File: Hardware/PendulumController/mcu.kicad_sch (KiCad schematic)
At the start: 21 parts, among them J201 ICSP, SW201 RESET, SW202 START_SW, SW203 STOP/MODE_SW, U201 ATmega328P, Y201 16mHz

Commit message: Fix DRC check
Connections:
- net SCL: no longer names the net of U201.28 (PC5)
- net SDA: no longer names the net of U201.27 (PC4)
- no-connect marks 7 -> 9
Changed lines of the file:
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@@
   (junction (at 59.69 86.995) (diameter 0) (color 0 0 0 0)
   )
+  (no_connect (at 57.785 81.915))
   (no_connect (at 27.305 56.515))
+  (no_connect (at 57.785 84.455))
   (no_connect (at 48.26 154.94))
   (no_connect (at 48.26 157.48))
@@
     (stroke (width 0) (type default) (color 0 0 0 0))
   )
-  (wire (pts (xy 66.675 84.455) (xy 57.785 84.455))
-    (stroke (width 0) (type default) (color 0 0 0 0))
-  )
   (wire (pts (xy 129.54 73.025) (xy 129.54 73.66))
     (stroke (width 0) (type default) (color 0 0 0 0))
@@
   )
   (polyline (pts (xy 13.335 173.355) (xy 64.77 173.355))
-    (stroke (width 0) (type default) (color 0 0 0 0))
-  )
-  (wire (pts (xy 66.675 81.915) (xy 57.785 81.915))
     (stroke (width 0) (type default) (color 0 0 0 0))
   )
@@
     (effects (font (size 1.27 1.27)) (justify right))
   )
-  (hierarchical_label "SCL" (shape output) (at 66.675 84.455 0)
-    (effects (font (size 1.27 1.27)) (justify left))
-  )
   (hierarchical_label "TFT_CS" (shape output) (at 81.28 104.775 0)
     (effects (font (size 1.27 1.27)) (justify left))
@@
     (effects (font (size 1.27 1.27)) (justify left))
   )
-  (hierarchical_label "SDA" (shape bidirectional) (at 66.675 81.915 0)
-    (effects (font (size 1.27 1.27)) (justify left))
-  )

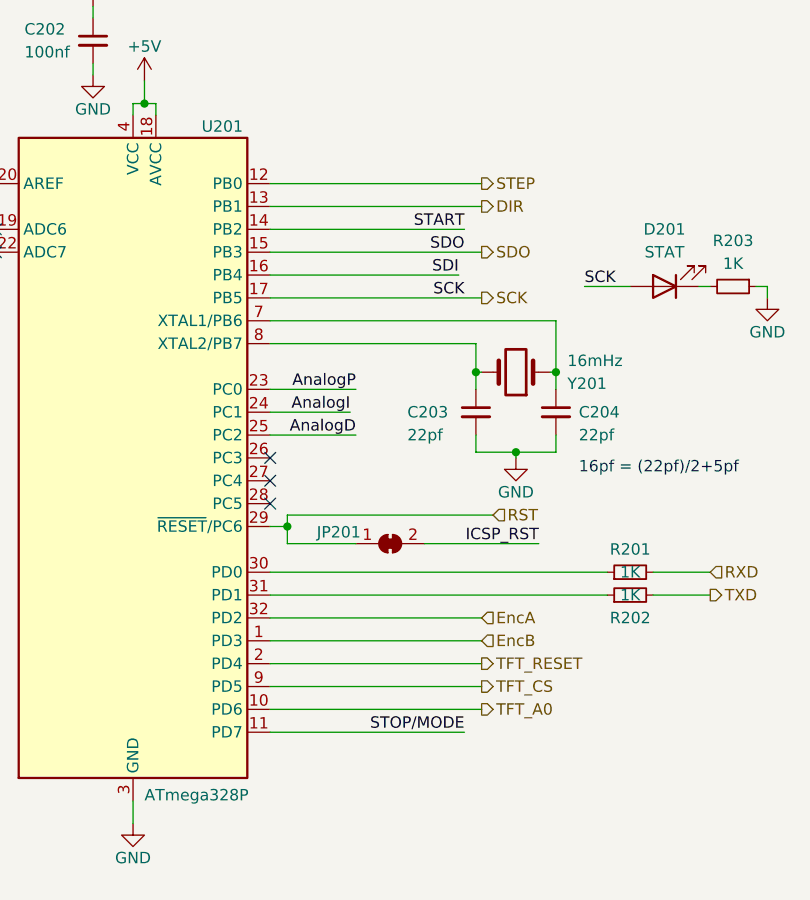
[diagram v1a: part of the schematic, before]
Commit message: Check backlight power circuit before printing
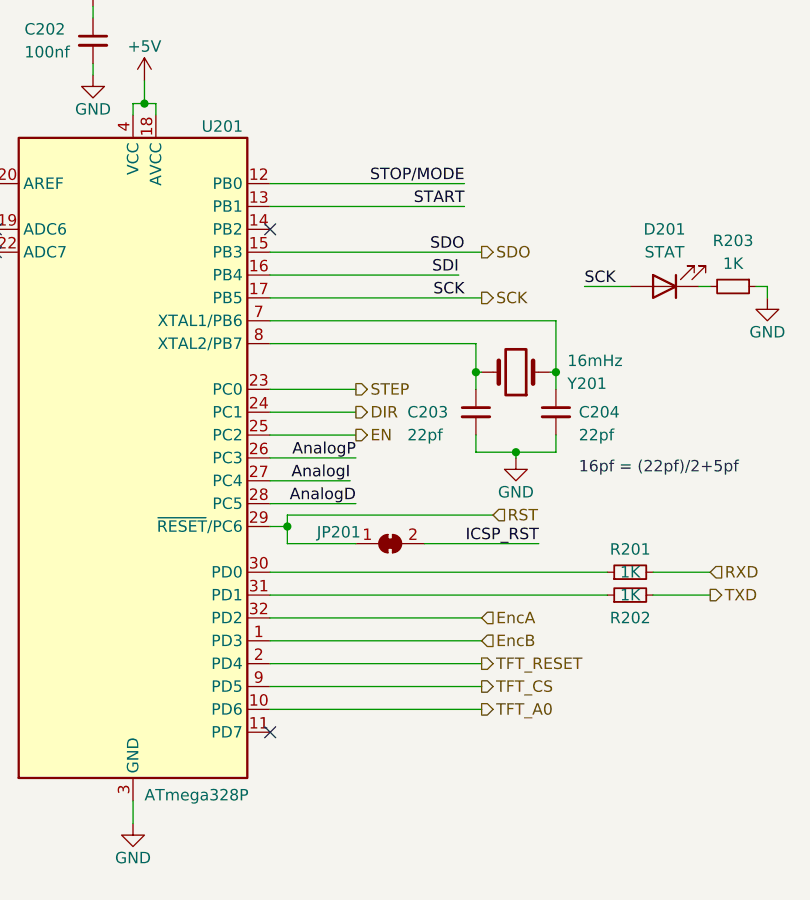
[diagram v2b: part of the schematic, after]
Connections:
- net AnalogD: now also U201.28 (PC5); no longer U201.25 (PC2)
- net AnalogI: now also U201.27 (PC4); no longer U201.24 (PC1)
- net AnalogP: now also U201.26 (PC3); no longer U201.23 (PC0)
- net DIR: now also U201.24 (PC1); no longer U201.13 (PB1)
- net START: now also U201.13 (PB1); no longer U201.14 (PB2)
- net STEP: now also U201.23 (PC0); no longer U201.12 (PB0)
- net STOP/MODE: now also U201.12 (PB0); no longer U201.11 (PD7)
- new net EN: U201.25 (PC2)
- no-connect marks 9 -> 8
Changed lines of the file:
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@@
   (junction (at 59.69 86.995) (diameter 0) (color 0 0 0 0)
   )
-  (no_connect (at 57.785 81.915))
   (no_connect (at 27.305 56.515))
-  (no_connect (at 57.785 84.455))
   (no_connect (at 48.26 154.94))
+  (no_connect (at 57.785 53.975))
+  (no_connect (at 57.785 109.855))
   (no_connect (at 48.26 157.48))
   (no_connect (at 48.26 152.4))
   (no_connect (at 35.56 152.4))
-  (no_connect (at 57.785 79.375))
   (no_connect (at 27.305 53.975))
-  (wire (pts (xy 57.785 48.895) (xy 81.28 48.895))
-    (stroke (width 0) (type default) (color 0 0 0 0))
-  )
   (wire (pts (xy 129.54 92.075) (xy 129.54 93.345))
     (stroke (width 0) (type default) (color 0 0 0 0))
@@
     (stroke (width 0) (type default) (color 0 0 0 0))
   )
-  (wire (pts (xy 57.785 71.755) (xy 67.31 71.755))
-    (stroke (width 0) (type default) (color 0 0 0 0))
-  )
   (wire (pts (xy 23.495 56.515) (xy 23.495 59.055))
     (stroke (width 0) (type default) (color 0 0 0 0))
   )
-  (wire (pts (xy 57.785 51.435) (xy 81.28 51.435))
-    (stroke (width 0) (type default) (color 0 0 0 0))
-  )
   (wire (pts (xy 45.085 40.005) (xy 43.815 40.005))
     (stroke (width 0) (type default) (color 0 0 0 0))
@@
     (stroke (width 0) (type default) (color 0 0 0 0))
   )
+  (wire (pts (xy 57.785 51.435) (xy 79.375 51.435))
+    (stroke (width 0) (type default) (color 0 0 0 0))
+  )
   (wire (pts (xy 80.645 69.85) (xy 81.28 69.85))
     (stroke (width 0) (type default) (color 0 0 0 0))
@@
     (stroke (width 0) (type default) (color 0 0 0 0))
   )
+  (wire (pts (xy 67.31 74.295) (xy 57.785 74.295))
+    (stroke (width 0) (type default) (color 0 0 0 0))
+  )
   (wire (pts (xy 129.54 81.28) (xy 129.54 81.915))
     (stroke (width 0) (type default) (color 0 0 0 0))
@@
     (stroke (width 0) (type default) (color 0 0 0 0))
   )
+  (wire (pts (xy 57.785 79.375) (xy 67.31 79.375))
+    (stroke (width 0) (type default) (color 0 0 0 0))
+  )
   (wire (pts (xy 154.305 27.305) (xy 173.355 27.305))
     (stroke (width 0) (type default) (color 0 0 0 0))
@@
     (stroke (width 0) (type default) (color 0 0 0 0))
   )
-  (wire (pts (xy 79.375 53.975) (xy 57.785 53.975))
-    (stroke (width 0) (type default) (color 0 0 0 0))
-  )
   (wire (pts (xy 187.96 41.91) (xy 187.96 44.45))
     (stroke (width 0) (type default) (color 0 0 0 0))
@@
     (stroke (width 0) (type default) (color 0 0 0 0))
   )
-  (wire (pts (xy 57.785 74.295) (xy 66.675 74.295))
-    (stroke (width 0) (type default) (color 0 0 0 0))
-  )
   (wire (pts (xy 24.13 154.94) (xy 35.56 154.94))
     (stroke (width 0) (type default) (color 0 0 0 0))
@@
     (stroke (width 0) (type default) (color 0 0 0 0))
   )
-  (wire (pts (xy 57.785 76.835) (xy 67.31 76.835))
-    (stroke (width 0) (type default) (color 0 0 0 0))
-  )
   (wire (pts (xy 80.645 69.85) (xy 80.645 71.755))
     (stroke (width 0) (type default) (color 0 0 0 0))
   )
+  (wire (pts (xy 57.785 84.455) (xy 67.31 84.455))
+    (stroke (width 0) (type default) (color 0 0 0 0))
+  )
   (wire (pts (xy 80.645 78.74) (xy 85.09 78.74))
     (stroke (width 0) (type default) (color 0 0 0 0))
@@
     (stroke (width 0) (type default) (color 0 0 0 0))
   )
+  (wire (pts (xy 79.375 48.895) (xy 57.785 48.895))
+    (stroke (width 0) (type default) (color 0 0 0 0))
+  )
   (wire (pts (xy 105.41 60.325) (xy 106.68 60.325))
     (stroke (width 0) (type default) (color 0 0 0 0))
@@
     (stroke (width 0) (type default) (color 0 0 0 0))
   )
+  (wire (pts (xy 67.31 71.755) (xy 57.785 71.755))
+    (stroke (width 0) (type default) (color 0 0 0 0))
+  )
   (polyline (pts (xy 119.38 13.335) (xy 119.38 137.16))
     (stroke (width 0) (type default) (color 0 0 0 0))
@@
     (stroke (width 0) (type default) (color 0 0 0 0))
   )
+  (wire (pts (xy 67.31 76.835) (xy 57.785 76.835))
+    (stroke (width 0) (type default) (color 0 0 0 0))
+  )
   (wire (pts (xy 48.26 160.02) (xy 50.165 160.02))
     (stroke (width 0) (type default) (color 0 0 0 0))
   )
-  (wire (pts (xy 79.375 109.855) (xy 57.785 109.855))
-    (stroke (width 0) (type default) (color 0 0 0 0))
-  )
   (wire (pts (xy 38.1 29.21) (xy 38.1 30.48))
     (stroke (width 0) (type default) (color 0 0 0 0))
   )
+  (wire (pts (xy 57.785 81.915) (xy 66.675 81.915))
+    (stroke (width 0) (type default) (color 0 0 0 0))
+  )
   (wire (pts (xy 81.28 99.695) (xy 57.785 99.695))
     (stroke (width 0) (type default) (color 0 0 0 0))
@@
     (effects (font (size 1.27 1.27)) (justify left bottom))
   )
+  (label "AnalogD" (at 67.31 84.455 180)
+    (effects (font (size 1.27 1.27)) (justify right bottom))
+  )
+  (label "AnalogI" (at 66.675 81.915 180)
+    (effects (font (size 1.27 1.27)) (justify right bottom))
+  )
   (label "SDO" (at 24.13 149.86 0)
     (effects (font (size 1.27 1.27)) (justify left bottom))
@@
     (effects (font (size 1.27 1.27)) (justify left bottom))
   )
-  (label "START" (at 79.375 53.975 180)
-    (effects (font (size 1.27 1.27)) (justify right bottom))
-  )
   (label "SDI" (at 24.13 160.02 0)
     (effects (font (size 1.27 1.27)) (justify left bottom))
   )
-  (label "STOP{slash}MODE" (at 79.375 109.855 180)
-    (effects (font (size 1.27 1.27)) (justify right bottom))
-  )
   (label "START" (at 154.305 27.305 0)
     (effects (font (size 1.27 1.27)) (justify left bottom))
@@
     (effects (font (size 1.27 1.27)) (justify right bottom))
   )
+  (label "STOP{slash}MODE" (at 79.375 48.895 180)
+    (effects (font (size 1.27 1.27)) (justify right bottom))
+  )
   (label "AnalogI" (at 140.97 77.47 180)
     (effects (font (size 1.27 1.27)) (justify right bottom))
   )
-  (label "AnalogP" (at 67.31 71.755 180)
-    (effects (font (size 1.27 1.27)) (justify right bottom))
-  )
   (label "SDI" (at 78.74 59.055 180)
     (effects (font (size 1.27 1.27)) (justify right bottom))
@@
     (effects (font (size 1.27 1.27)) (justify right bottom))
   )
+  (label "START" (at 79.375 51.435 180)
+    (effects (font (size 1.27 1.27)) (justify right bottom))
+  )
+  (label "AnalogP" (at 67.31 79.375 180)
+    (effects (font (size 1.27 1.27)) (justify right bottom))
+  )
   (label "ICSP_RST" (at 24.13 154.94 0)
     (effects (font (size 1.27 1.27)) (justify left bottom))
   )
-  (label "AnalogI" (at 66.675 74.295 180)
-    (effects (font (size 1.27 1.27)) (justify right bottom))
-  )
-  (label "AnalogD" (at 67.31 76.835 180)
-    (effects (font (size 1.27 1.27)) (justify right bottom))
-  )
   (label "SCK" (at 79.375 61.595 180)
     (effects (font (size 1.27 1.27)) (justify right bottom))
@@
   )
   (hierarchical_label "RST" (shape input) (at 82.55 85.725 0)
+    (effects (font (size 1.27 1.27)) (justify left))
+  )
+  (hierarchical_label "DIR" (shape output) (at 67.31 74.295 0)
     (effects (font (size 1.27 1.27)) (justify left))
   )
@@
     (effects (font (size 1.27 1.27)) (justify left))
   )
-  (hierarchical_label "DIR" (shape output) (at 81.28 51.435 0)
-    (effects (font (size 1.27 1.27)) (justify left))
-  )
   (hierarchical_label "EncA" (shape input) (at 81.28 97.155 0)
     (effects (font (size 1.27 1.27)) (justify left))
@@
     (effects (font (size 1.27 1.27)) (justify left))
   )
-  (hierarchical_label "STEP" (shape output) (at 81.28 48.895 0)
-    (effects (font (size 1.27 1.27)) (justify left))
-  )
+  (hierarchical_label "STEP" (shape output) (at 67.31 71.755 0)
+    (effects (font (size 1.27 1.27)) (justify left))
+  )
+  (hierarchical_label "EN" (shape output) (at 67.31 76.835 0)
+    (effects (font (size 1.27 1.27)) (justify left))
+  )
